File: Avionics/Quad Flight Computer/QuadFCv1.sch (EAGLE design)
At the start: 91 parts, among them J1 10104111_MICROUSBAB, SW1 2-1437565-9, U1 TM4C123GH6PZ, U2 74LVC4245APW, U3 ATMEGA32U2-MU, U4 SPI_PPM, U5 MPU-6000, U6 HMC5883LSMD, U7 MS5611-01BA, U8 74AUP1G19GW, U9 S25FL127S, X1 HWB, Y1 32.768KHZ, Y2 AWSCR-20.00CW-T, Y3 PRQC16.00SR5010X000

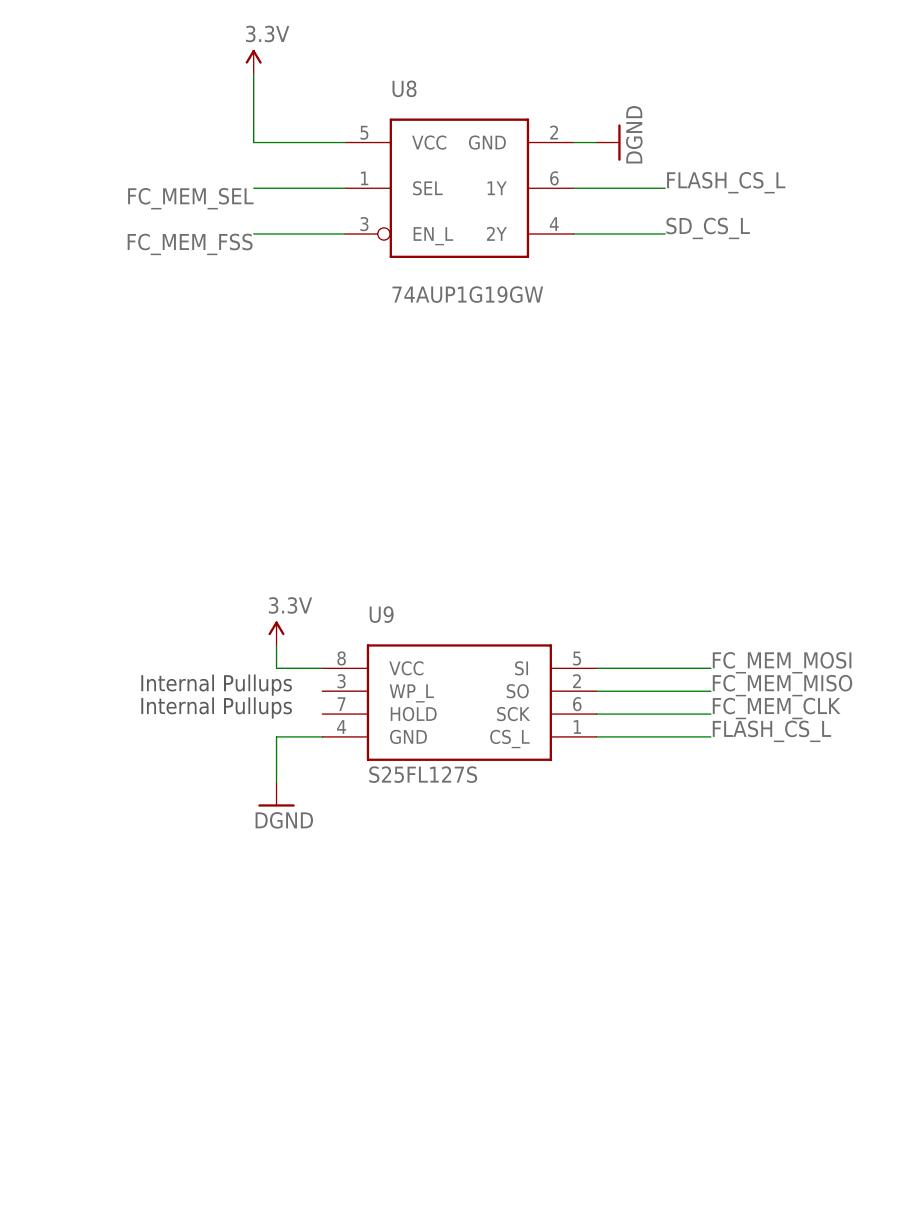
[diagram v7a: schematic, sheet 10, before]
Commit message: Added Micro SD Card slot
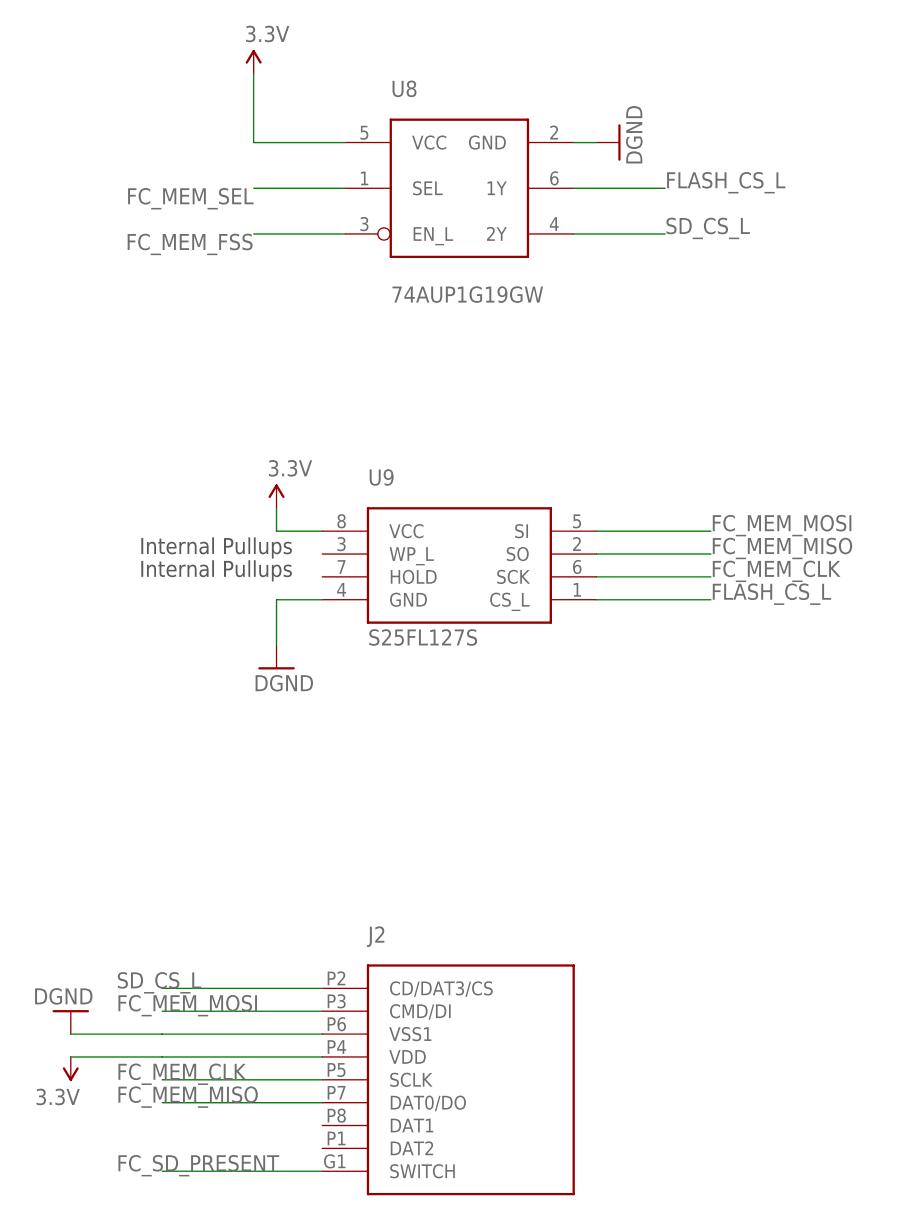
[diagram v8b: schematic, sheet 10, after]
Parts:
- added J2: 1050270001, Shared Libraries:1050270001
- added R42, R43: 2.2k, Shared Libraries:RESISTOR0603-RES
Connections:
- new net FC_SD_PRESENT: J2.SWITCH
- net 3.3V: now also J2.VDD, R42.2, R43.2
- net FC_MEM_CLK: now also J2.SCLK
- net FC_MEM_MISO: now also J2.DAT0/DO
- net FC_MEM_MOSI: now also J2.CMD/DI
- net FC_SENSE_SCL: now also R42.1
- net FC_SENSE_SDA: now also R43.1
- net GND: now also J2.VSS1
- net SD_CS_L: now also J2.CD/DAT3/CS
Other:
- moved on the sheet: U9
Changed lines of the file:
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@@
 <part name="SUPPLY21" library="SparkFun-Aesthetics" deviceset="3.3V" device=""/>
 <part name="GND32" library="SparkFun-Aesthetics" deviceset="DGND" device=""/>
+<part name="R42" library="Shared Libraries" deviceset="RESISTOR" device="0603-RES" value="2.2k"/>
+<part name="R43" library="Shared Libraries" deviceset="RESISTOR" device="0603-RES" value="2.2k"/>
+<part name="SUPPLY22" library="SparkFun-Aesthetics" deviceset="3.3V" device=""/>
+<part name="J2" library="Shared Libraries" deviceset="1050270001" device=""/>
+<part name="GND34" library="SparkFun-Aesthetics" deviceset="DGND" device=""/>
+<part name="SUPPLY23" library="SparkFun-Aesthetics" deviceset="3.3V" device=""/>
 </parts>
 <sheets>
@@
 <instance part="C9" gate="G$1" x="205.74" y="-109.22"/>
 <instance part="GND12" gate="G$1" x="205.74" y="-116.84" rot="MR0"/>
+<instance part="R42" gate="G$1" x="-30.48" y="-10.16" rot="R90"/>
+<instance part="R43" gate="G$1" x="-38.1" y="-10.16" rot="R90"/>
+<instance part="SUPPLY22" gate="G$1" x="-38.1" y="-5.08"/>
 </instances>
 <busses>
@@
 <pinref part="SUPPLY4" gate="G$1" pin="3.3V"/>
 </segment>
+<segment>
+<pinref part="R43" gate="G$1" pin="2"/>
+<pinref part="R42" gate="G$1" pin="2"/>
+<wire x1="-38.1" y1="-5.08" x2="-30.48" y2="-5.08" width="0.1524" layer="91"/>
+<pinref part="SUPPLY22" gate="G$1" pin="3.3V"/>
+<junction x="-38.1" y="-5.08"/>
+</segment>
 </net>
 <net name="GND" class="0">
@@
 <wire x1="17.78" y1="-17.78" x2="-12.7" y2="-17.78" width="0.1524" layer="91"/>
 <label x="-12.7" y="-17.78" size="1.778" layer="95"/>
+<pinref part="R42" gate="G$1" pin="1"/>
+<wire x1="-12.7" y1="-17.78" x2="-30.48" y2="-17.78" width="0.1524" layer="91"/>
+<wire x1="-30.48" y1="-17.78" x2="-30.48" y2="-15.24" width="0.1524" layer="91"/>
 </segment>
 </net>
@@
 <wire x1="-12.7" y1="-20.32" x2="17.78" y2="-20.32" width="0.1524" layer="91"/>
 <label x="-12.7" y="-20.32" size="1.778" layer="95"/>
+<pinref part="R43" gate="G$1" pin="1"/>
+<wire x1="-38.1" y1="-15.24" x2="-38.1" y2="-20.32" width="0.1524" layer="91"/>
+<wire x1="-38.1" y1="-20.32" x2="-12.7" y2="-20.32" width="0.1524" layer="91"/>
 </segment>
 </net>
@@
 <wire x1="-88.9" y1="27.94" x2="-88.9" y2="30.48" width="0.1524" layer="91"/>
 <pinref part="SUPPLY7" gate="G$1" pin="3.3V"/>
+<junction x="-88.9" y="27.94"/>
 </segment>
 <segment>
@@
 <wire x1="-86.36" y1="-71.12" x2="-81.28" y2="-71.12" width="0.1524" layer="91"/>
 <wire x1="-81.28" y1="-71.12" x2="-81.28" y2="-63.5" width="0.1524" layer="91"/>
+<junction x="-91.44" y="-71.12"/>
+<junction x="-86.36" y="-71.12"/>
 </segment>
 <segment>
@@
 <pinref part="GND27" gate="G$1" pin="GND"/>
 <junction x="-17.78" y="-10.16"/>
+<junction x="-22.86" y="-15.24"/>
 </segment>
 </net>
@@
 <description>Memory</description>
 <plain>
-<text x="-35.56" y="-53.34" size="1.778" layer="97">Internal Pullups</text>
-<text x="-35.56" y="-55.88" size="1.778" layer="97">Internal Pullups</text>
+<text x="-35.56" y="-38.1" size="1.778" layer="97">Internal Pullups</text>
+<text x="-35.56" y="-40.64" size="1.778" layer="97">Internal Pullups</text>
 </plain>
 <instances>
@@
 <instance part="GND31" gate="G$1" x="17.78" y="7.62" rot="R90"/>
 <instance part="SUPPLY15" gate="G$1" x="-22.86" y="15.24"/>
-<instance part="U9" gate="G$1" x="0" y="-55.88"/>
-<instance part="SUPPLY21" gate="G$1" x="-20.32" y="-48.26"/>
-<instance part="GND32" gate="G$1" x="-20.32" y="-66.04"/>
+<instance part="U9" gate="G$1" x="0" y="-40.64"/>
+<instance part="SUPPLY21" gate="G$1" x="-20.32" y="-33.02"/>
+<instance part="GND32" gate="G$1" x="-20.32" y="-50.8"/>
+<instance part="J2" gate="G$1" x="-7.62" y="-96.52"/>
+<instance part="GND34" gate="G$1" x="-43.18" y="-88.9" rot="R180"/>
+<instance part="SUPPLY23" gate="G$1" x="-43.18" y="-93.98" rot="R180"/>
 </instances>
 <busses>
@@
 <pinref part="U9" gate="G$1" pin="GND"/>
 <pinref part="GND32" gate="G$1" pin="GND"/>
-<wire x1="-15.24" y1="-58.42" x2="-20.32" y2="-58.42" width="0.1524" layer="91"/>
-<wire x1="-20.32" y1="-58.42" x2="-20.32" y2="-63.5" width="0.1524" layer="91"/>
+<wire x1="-15.24" y1="-43.18" x2="-20.32" y2="-43.18" width="0.1524" layer="91"/>
+<wire x1="-20.32" y1="-43.18" x2="-20.32" y2="-48.26" width="0.1524" layer="91"/>
+</segment>
+<segment>
+<pinref part="J2" gate="G$1" pin="VSS1"/>
+<wire x1="-15.24" y1="-91.44" x2="-33.02" y2="-91.44" width="0.1524" layer="91"/>
+<pinref part="GND34" gate="G$1" pin="GND"/>
+<wire x1="-33.02" y1="-91.44" x2="-43.18" y2="-91.44" width="0.1524" layer="91"/>
 </segment>
 </net>
@@
 <pinref part="U9" gate="G$1" pin="VCC"/>
 <pinref part="SUPPLY21" gate="G$1" pin="3.3V"/>
-<wire x1="-15.24" y1="-50.8" x2="-20.32" y2="-50.8" width="0.1524" layer="91"/>
-<wire x1="-20.32" y1="-50.8" x2="-20.32" y2="-48.26" width="0.1524" layer="91"/>
+<wire x1="-15.24" y1="-35.56" x2="-20.32" y2="-35.56" width="0.1524" layer="91"/>
+<wire x1="-20.32" y1="-35.56" x2="-20.32" y2="-33.02" width="0.1524" layer="91"/>
+</segment>
+<segment>
+<pinref part="J2" gate="G$1" pin="VDD"/>
+<wire x1="-15.24" y1="-93.98" x2="-33.02" y2="-93.98" width="0.1524" layer="91"/>
+<pinref part="SUPPLY23" gate="G$1" pin="3.3V"/>
+<wire x1="-43.18" y1="-93.98" x2="-33.02" y2="-93.98" width="0.1524" layer="91"/>
 </segment>
 </net>
@@
 <segment>
 <pinref part="U9" gate="G$1" pin="CS_L"/>
-<wire x1="15.24" y1="-58.42" x2="27.94" y2="-58.42" width="0.1524" layer="91"/>
-<label x="27.94" y="-58.42" size="1.778" layer="95"/>
+<wire x1="15.24" y1="-43.18" x2="27.94" y2="-43.18" width="0.1524" layer="91"/>
+<label x="27.94" y="-43.18" size="1.778" layer="95"/>
 </segment>
 </net>
@@
 <label x="22.86" y="-2.54" size="1.778" layer="95"/>
 </segment>
+<segment>
+<pinref part="J2" gate="G$1" pin="CD/DAT3/CS"/>
+<wire x1="-15.24" y1="-86.36" x2="-33.02" y2="-86.36" width="0.1524" layer="91"/>
+<label x="-38.1" y="-86.36" size="1.778" layer="95"/>
+</segment>
 </net>
 <net name="FC_MEM_MOSI" class="0">
 <segment>
 <pinref part="U9" gate="G$1" pin="SI"/>
-<wire x1="15.24" y1="-50.8" x2="27.94" y2="-50.8" width="0.1524" layer="91"/>
-<label x="27.94" y="-50.8" size="1.778" layer="95"/>
+<wire x1="15.24" y1="-35.56" x2="27.94" y2="-35.56" width="0.1524" layer="91"/>
+<label x="27.94" y="-35.56" size="1.778" layer="95"/>
+</segment>
+<segment>
+<pinref part="J2" gate="G$1" pin="CMD/DI"/>
+<wire x1="-15.24" y1="-88.9" x2="-33.02" y2="-88.9" width="0.1524" layer="91"/>
+<label x="-38.1" y="-88.9" size="1.778" layer="95"/>
 </segment>
 </net>
@@
 <segment>
 <pinref part="U9" gate="G$1" pin="SO"/>
-<wire x1="15.24" y1="-53.34" x2="27.94" y2="-53.34" width="0.1524" layer="91"/>
-<label x="27.94" y="-53.34" size="1.778" layer="95"/>
+<wire x1="15.24" y1="-38.1" x2="27.94" y2="-38.1" width="0.1524" layer="91"/>
+<label x="27.94" y="-38.1" size="1.778" layer="95"/>
+</segment>
+<segment>
+<pinref part="J2" gate="G$1" pin="DAT0/DO"/>
+<wire x1="-15.24" y1="-99.06" x2="-33.02" y2="-99.06" width="0.1524" layer="91"/>
+<label x="-38.1" y="-99.06" size="1.778" layer="95"/>
 </segment>
 </net>
@@
 <segment>
 <pinref part="U9" gate="G$1" pin="SCK"/>
-<wire x1="15.24" y1="-55.88" x2="27.94" y2="-55.88" width="0.1524" layer="91"/>
-<label x="27.94" y="-55.88" size="1.778" layer="95"/>
-</segment>
-</net>
+<wire x1="15.24" y1="-40.64" x2="27.94" y2="-40.64" width="0.1524" layer="91"/>
+<label x="27.94" y="-40.64" size="1.778" layer="95"/>
+</segment>
+<segment>
+<pinref part="J2" gate="G$1" pin="SCLK"/>
+<wire x1="-15.24" y1="-96.52" x2="-33.02" y2="-96.52" width="0.1524" layer="91"/>
+<label x="-38.1" y="-96.52" size="1.778" layer="95"/>
+</segment>
+</net>
+<net name="FC_SD_PRESENT" class="0">
+<segment>
+<pinref part="J2" gate="G$1" pin="SWITCH"/>
+<wire x1="-15.24" y1="-106.68" x2="-33.02" y2="-106.68" width="0.1524" layer="91"/>
+<label x="-38.1" y="-106.68" size="1.778" layer="95"/>
+</segment>
+</net>
